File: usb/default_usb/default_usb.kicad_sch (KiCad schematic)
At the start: 4 parts

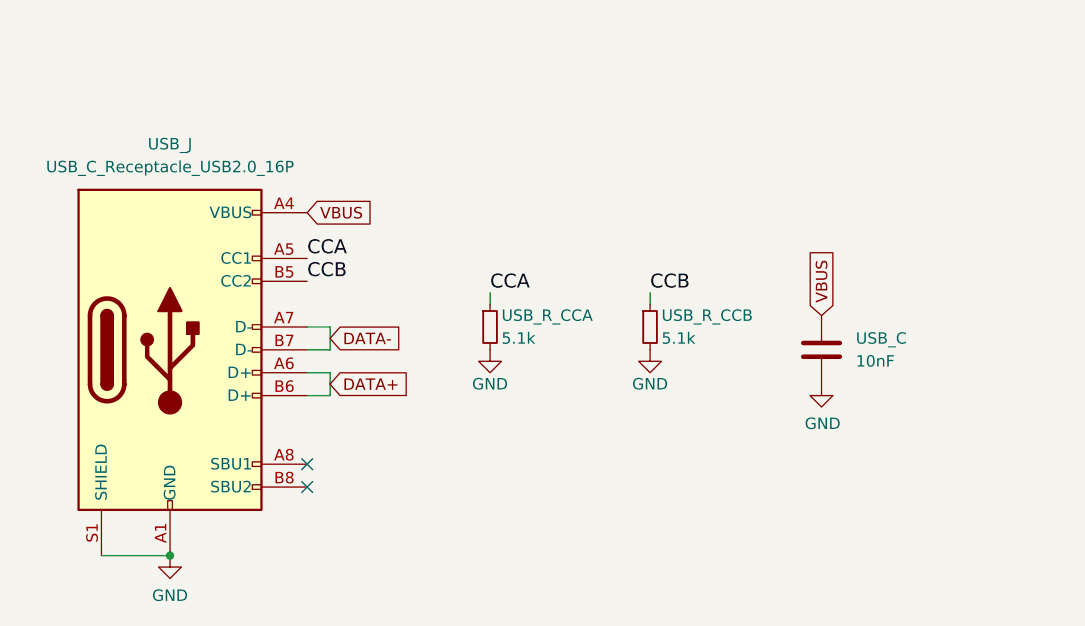
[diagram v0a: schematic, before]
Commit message: upgrade modules with kicad_sh and kicad_pcb
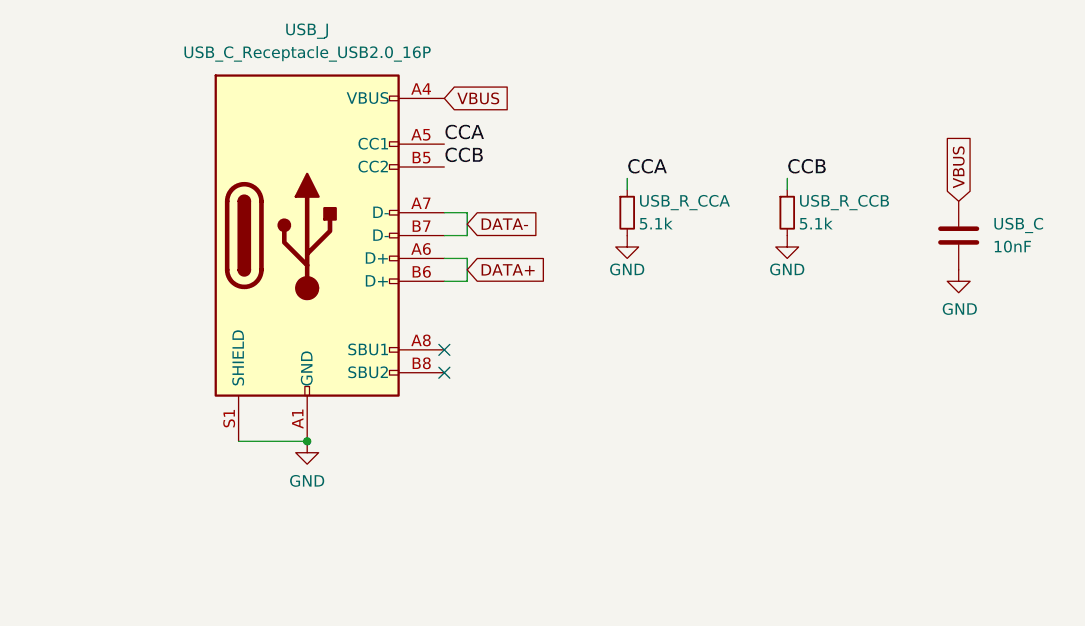
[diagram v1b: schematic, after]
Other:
- moved on the sheet: USB_C, USB_J, USB_R_CCA, USB_R_CCB

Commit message: update usb_c template
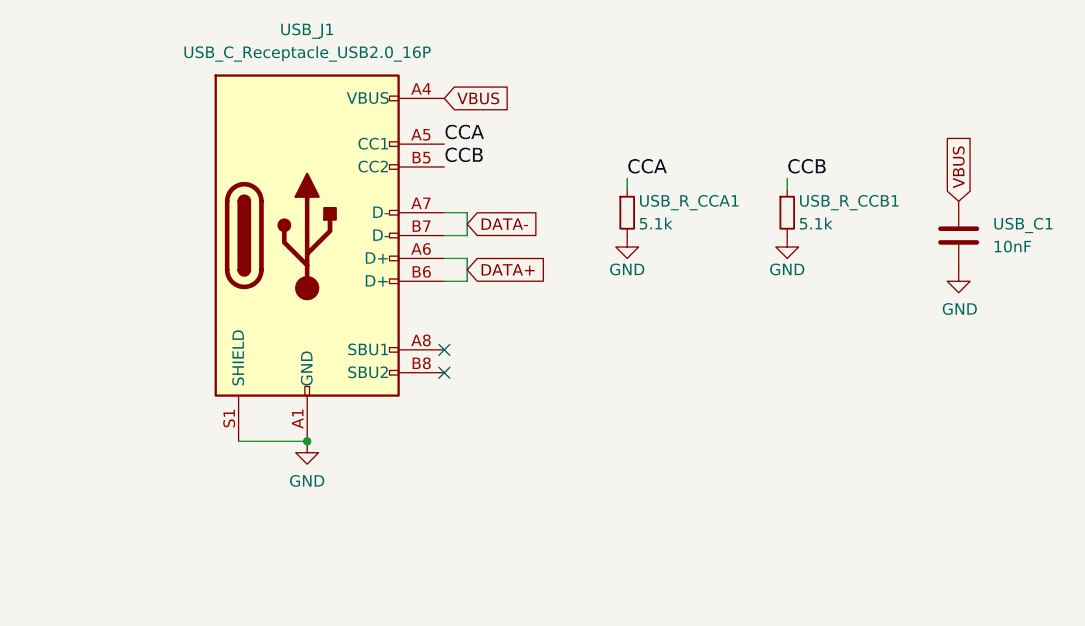
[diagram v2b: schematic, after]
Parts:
- USB_C1: renamed from USB_C; footprint Capacitor_SMD:C_0805_2012Metric_Pad1.18x1.45mm_HandSolder -> ErgoCai.pretty:C_0805_2012Metric_Pad1.18x1.45mm_HandSolder
- renumbered USB_J to USB_J1, USB_R_CCA to USB_R_CCA1, USB_R_CCB to USB_R_CCB1
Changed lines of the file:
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@@
 		(on_board yes)
 		(dnp no)
-		(property "Reference" "#PWR?"
+		(property "Reference" "#PWR0102"
 			(at 85.09 128.27 0)
 			(effects
@@
 			(project "1099-INT 2023 - Tax Form"
 				(path "/432d8d65-9222-4b2b-986b-9da987eb142e"
-					(reference "#PWR?")
+					(reference "#PWR0102")
 					(unit 1)
 				)
@@
 		(on_board yes)
 		(dnp no)
-		(property "Reference" "USB_R_CCB"
+		(property "Reference" "USB_R_CCB1"
 			(at 139.7 95.2499 0)
 			(effects
@@
 			(project "1099-INT 2023 - Tax Form"
 				(path "/432d8d65-9222-4b2b-986b-9da987eb142e"
-					(reference "USB_R_CCB")
+					(reference "USB_R_CCB1")
 					(unit 1)
 				)
@@
 		(on_board yes)
 		(dnp no)
-		(property "Reference" "#PWR?"
+		(property "Reference" "#PWR0104"
 			(at 138.43 105.41 0)
 			(effects
@@
 			(project "1099-INT 2023 - Tax Form"
 				(path "/432d8d65-9222-4b2b-986b-9da987eb142e"
-					(reference "#PWR?")
+					(reference "#PWR0104")
 					(unit 1)
 				)
@@
 		(on_board yes)
 		(dnp no)
-		(property "Reference" "#PWR?"
+		(property "Reference" "#PWR0101"
 			(at 120.65 105.41 0)
 			(effects
@@
 			(project "1099-INT 2023 - Tax Form"
 				(path "/432d8d65-9222-4b2b-986b-9da987eb142e"
-					(reference "#PWR?")
+					(reference "#PWR0101")
 					(unit 1)
 				)
@@
 		(dnp no)
 		(fields_autoplaced yes)
-		(property "Reference" "USB_J"
+		(property "Reference" "USB_J1"
 			(at 85.09 76.2 0)
 			(effects
@@
 			(project "1099-INT 2023 - Tax Form"
 				(path "/432d8d65-9222-4b2b-986b-9da987eb142e"
-					(reference "USB_J")
+					(reference "USB_J1")
 					(unit 1)
 				)
@@
 		(dnp no)
 		(fields_autoplaced yes)
-		(property "Reference" "USB_C"
+		(property "Reference" "USB_C1"
 			(at 161.29 97.7899 0)
 			(effects
@@
 			)
 		)
-		(property "Footprint" "Capacitor_SMD:C_0805_2012Metric_Pad1.18x1.45mm_HandSolder"
+		(property "Footprint" "ErgoCai.pretty:C_0805_2012Metric_Pad1.18x1.45mm_HandSolder"
 			(at 156.5148 95.25 0)
 			(effects
@@
 			)
 		)
-		(property "Description" "Unpolarized capacitor"
+		(property "Description" ""
 			(at 157.48 99.06 0)
 			(effects
@@
 			(project "1099-INT 2023 - Tax Form"
 				(path "/432d8d65-9222-4b2b-986b-9da987eb142e"
-					(reference "USB_C")
+					(reference "USB_C1")
 					(unit 1)
 				)
@@
 		(dnp no)
 		(fields_autoplaced yes)
-		(property "Reference" "#PWR?"
+		(property "Reference" "#PWR0103"
 			(at 157.48 109.22 0)
 			(effects
@@
 			(project "1099-INT 2023 - Tax Form"
 				(path "/432d8d65-9222-4b2b-986b-9da987eb142e"
-					(reference "#PWR?")
+					(reference "#PWR0103")
 					(unit 1)
 				)
@@
 		(on_board yes)
 		(dnp no)
-		(property "Reference" "USB_R_CCA"
+		(property "Reference" "USB_R_CCA1"
 			(at 121.92 95.2499 0)
 			(effects
@@
 			(project "1099-INT 2023 - Tax Form"
 				(path "/432d8d65-9222-4b2b-986b-9da987eb142e"
-					(reference "USB_R_CCA")
-					(unit 1)
-				)
+					(reference "USB_R_CCA1")
+					(unit 1)
+				)
